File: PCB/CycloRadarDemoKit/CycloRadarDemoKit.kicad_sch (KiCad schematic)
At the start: 7 parts, among them J101 I2C conn, J102 CAN, J103 100BASE-T1, J104 Radar debug, U101 RADAR POGO pins

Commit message: starting the mockup
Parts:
- added R103: 120, Resistor_SMD:R_0603_1608Metric, symbol Device:R
- J102: footprint (none) -> Connector_Molex:Molex_39501-1003; symbol Connector_Generic:Conn_01x02 -> Connector_Generic:Conn_01x03; Mouser (none) -> 538-39501-1003
- J103: footprint (none) -> Connector_Molex:Molex_KK-254_AE-6410-04A_1x04_P2.54mm_Vertical; symbol Connector_Generic:Conn_01x02 -> Connector_Generic:Conn_01x04; Mouser (none) -> 538-34793-0040; Note (none) -> Wrong footprint
- J104: now not fitted
- U101: footprint alps_modules:ALPS Generic Radar 5 -> alps_modules:ALPS_USRR5
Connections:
- net CANH: now also J102.3 (Pin_3), R103.1; no longer J102.2 (Pin_2)
- net CANL: now also R103.2
- net ETH_H: now also J103.3 (Pin_3); no longer J103.2 (Pin_2)
- net ETH_L: now also J103.2 (Pin_2); no longer J103.1 (Pin_1)
- net GND: now also J102.2 (Pin_2)
- no-connect marks 9 -> 11
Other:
- moved on the sheet: J101, U101

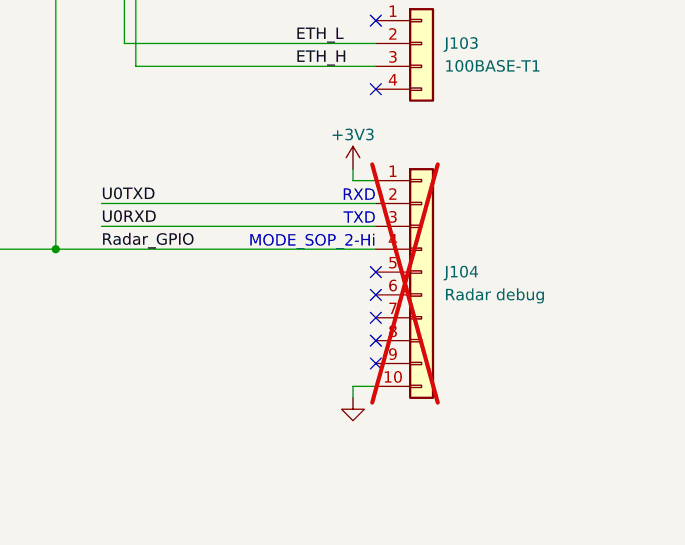
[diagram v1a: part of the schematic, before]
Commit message: layout mockup done
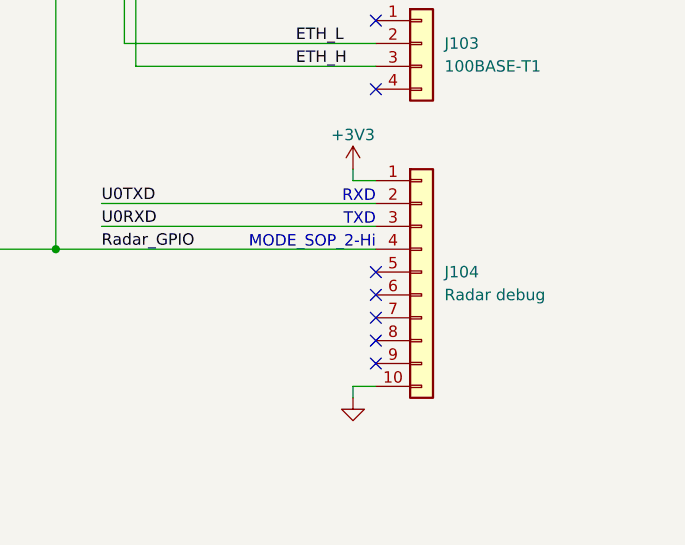
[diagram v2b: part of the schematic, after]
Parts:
- J104: now fitted
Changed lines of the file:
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@@
   )
   (symbol (lib_id "Connector_Generic:Conn_01x10") (at 257.81 135.89 0) (unit 1)
-    (in_bom yes) (on_board yes) (dnp yes) (fields_autoplaced)
+    (in_bom yes) (on_board yes) (dnp no) (fields_autoplaced)
     (property "Reference" "J104" (at 260.35 135.89 0)
       (effects (font (size 1.27 1.27)) (justify left))

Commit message: PCB, 3Dmodel
mockup PCB version done, schcematic exported to latex, 3D model generated and exported to latex
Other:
- note added: "All GND symbols refer to same ground"
- title: Safety Ride Radar Sensor -> Radar Safety Sensor
- moved on the sheet: J101, J102, J103, J104, R101, R102, R103, U101

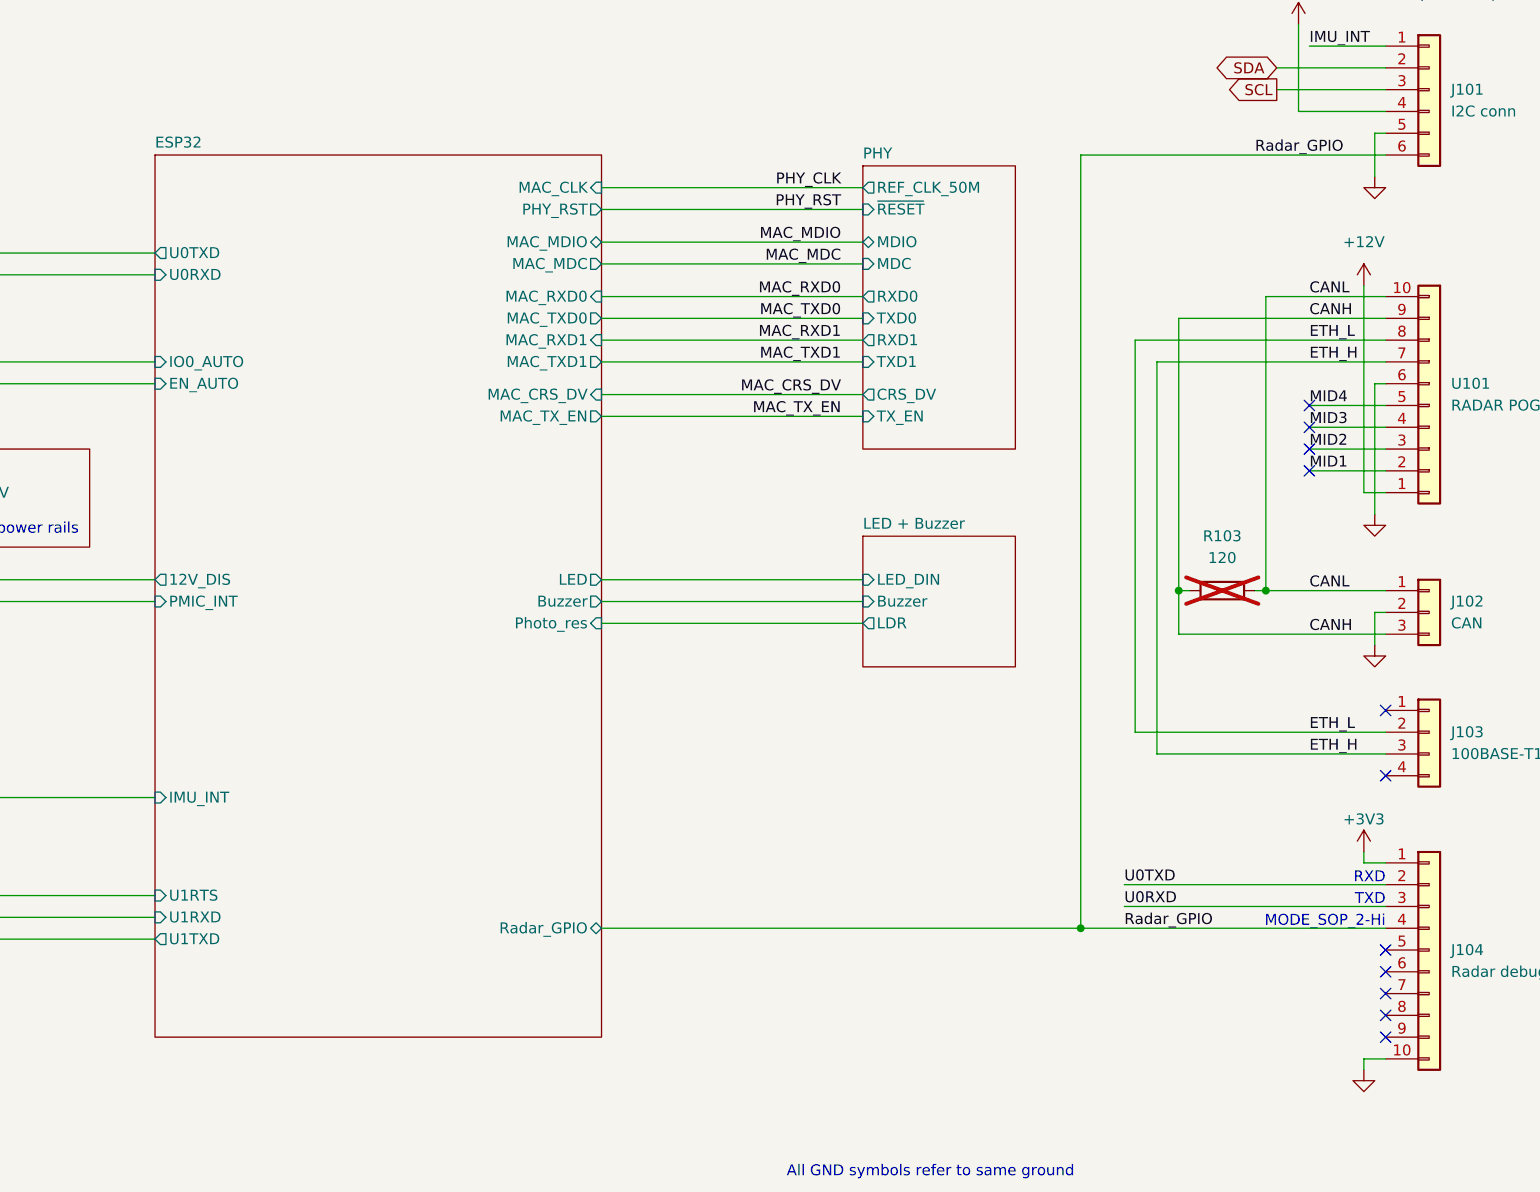
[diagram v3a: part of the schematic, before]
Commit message: sortingAbbr, cosmetics schematic, export schematic to thesis
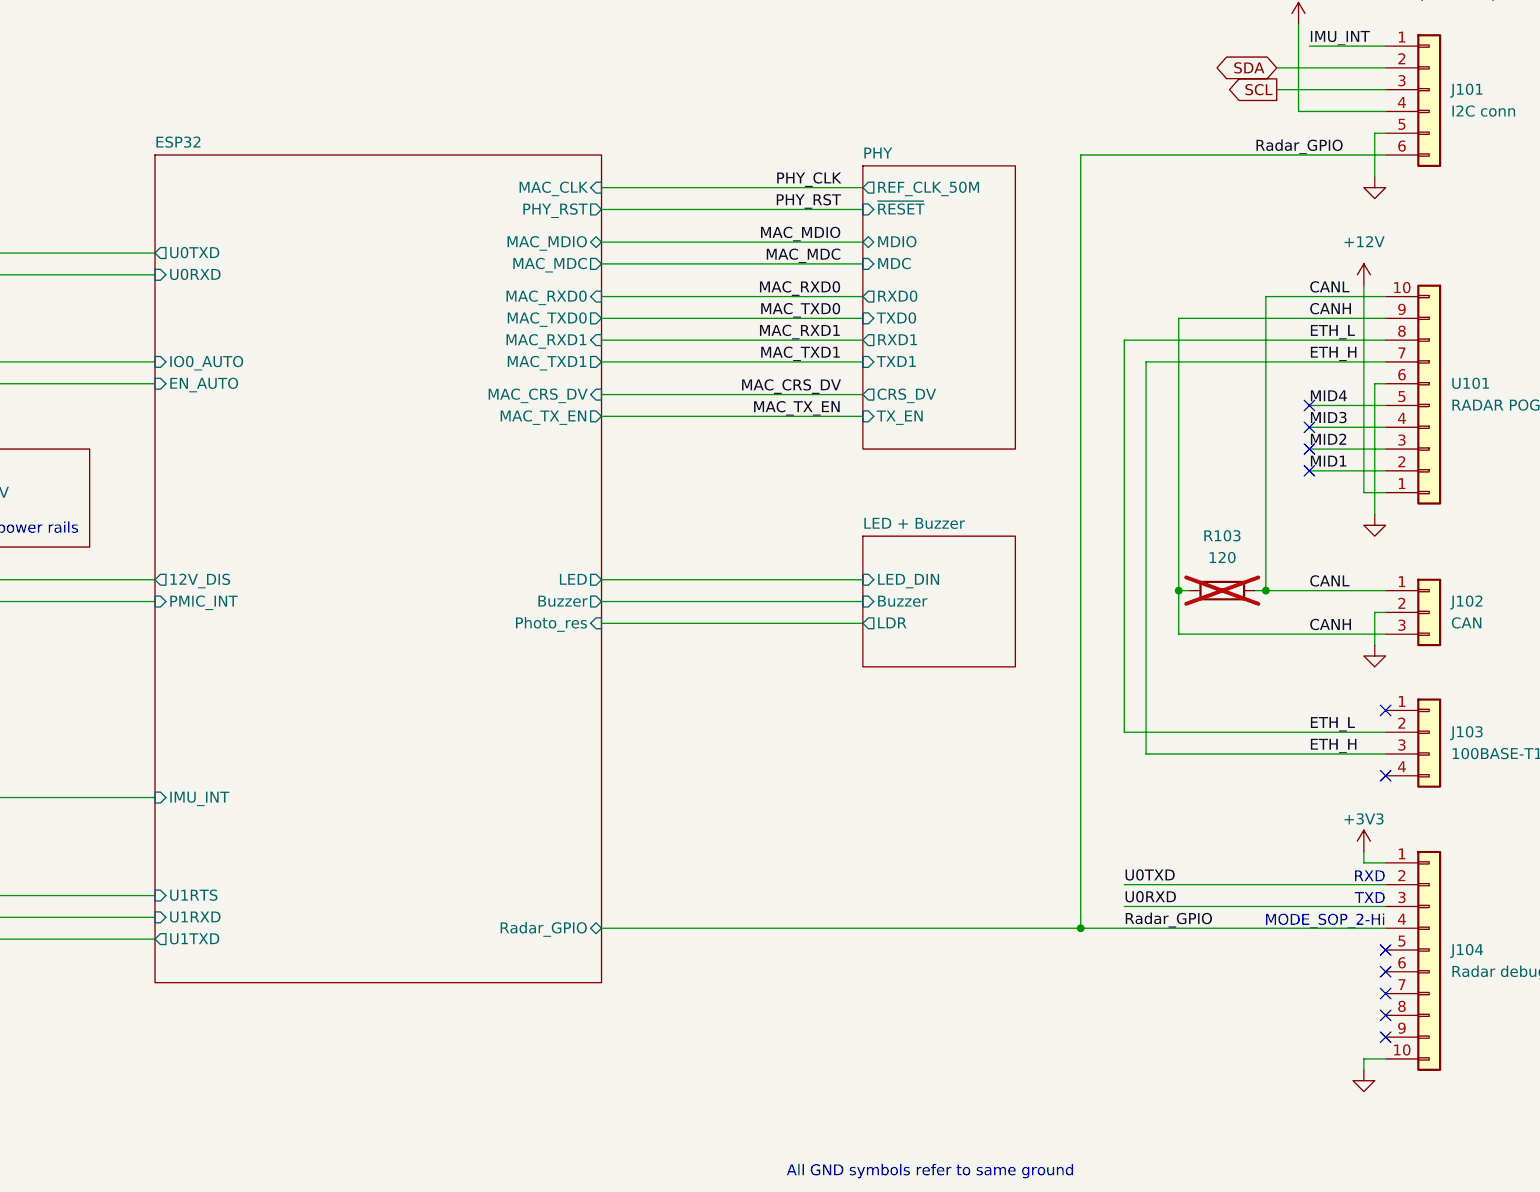
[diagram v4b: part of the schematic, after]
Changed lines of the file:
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@@
     (title "Radar Safety Sensor")
     (date "2023-12-20")
-    (rev "Rev.: 1")
+    (rev "Rev.: 1.0")
     (company "ALPS Electric Czech, s.r.o.")
     (comment 1 "Designed by Martin Tavoda")
@@
     (stroke (width 0) (type default))
   )
-  (wire (pts (xy 217.17 111.76) (xy 246.38 111.76))
+  (wire (pts (xy 215.9 111.76) (xy 246.38 111.76))
     (stroke (width 0) (type default))
   )
@@
     (stroke (width 0) (type default))
   )
-  (wire (pts (xy 219.71 114.3) (xy 219.71 68.58))
+  (wire (pts (xy 218.44 114.3) (xy 218.44 68.58))
     (stroke (width 0) (type default))
   )
@@
     (stroke (width 0) (type default))
   )
-  (wire (pts (xy 217.17 111.76) (xy 217.17 66.04))
+  (wire (pts (xy 215.9 111.76) (xy 215.9 66.04))
     (stroke (width 0) (type default))
   )
@@
     (stroke (width 0) (type default))
   )
-  (wire (pts (xy 219.71 68.58) (xy 246.38 68.58))
+  (wire (pts (xy 218.44 68.58) (xy 246.38 68.58))
     (stroke (width 0) (type default))
   )
@@
     (stroke (width 0) (type default))
   )
-  (wire (pts (xy 217.17 66.04) (xy 246.38 66.04))
+  (wire (pts (xy 215.9 66.04) (xy 246.38 66.04))
     (stroke (width 0) (type default))
   )
@@
     (stroke (width 0) (type default))
   )
-  (wire (pts (xy 219.71 114.3) (xy 246.38 114.3))
+  (wire (pts (xy 218.44 114.3) (xy 246.38 114.3))
     (stroke (width 0) (type default))
   )
@@
     )
   )
-  (sheet (at 102.87 44.45) (size 52.07 102.87) (fields_autoplaced)
+  (sheet (at 102.87 44.45) (size 52.07 96.52) (fields_autoplaced)
     (stroke (width 0.1524) (type solid))
     (fill (color 0 0 0 0.1000))
@@
       (effects (font (size 1.27 1.27)) (justify left bottom))
     )
-    (property "Sheetfile" "ESP32.kicad_sch" (at 102.87 147.9046 0)
+    (property "Sheetfile" "ESP32.kicad_sch" (at 102.87 141.5546 0)
       (effects (font (size 1.27 1.27)) (justify left top) hide)
     )
@@
     (instances
       (project "CycloRadarDemoKit"
-        (path "/c2cd7ca4-4652-4b3d-a3a8-1cfa66cb11e9" (page "8"))
+        (path "/c2cd7ca4-4652-4b3d-a3a8-1cfa66cb11e9" (page "2"))
       )
     )
@@
     (instances
       (project "CycloRadarDemoKit"
-        (path "/c2cd7ca4-4652-4b3d-a3a8-1cfa66cb11e9" (page "7"))
+        (path "/c2cd7ca4-4652-4b3d-a3a8-1cfa66cb11e9" (page "8"))
       )
     )
@@
     (instances
       (project "CycloRadarDemoKit"
-        (path "/c2cd7ca4-4652-4b3d-a3a8-1cfa66cb11e9" (page "2"))
+        (path "/c2cd7ca4-4652-4b3d-a3a8-1cfa66cb11e9" (page "3"))
       )
     )
@@
     (instances
       (project "CycloRadarDemoKit"
-        (path "/c2cd7ca4-4652-4b3d-a3a8-1cfa66cb11e9" (page "4"))
+        (path "/c2cd7ca4-4652-4b3d-a3a8-1cfa66cb11e9" (page "7"))
       )
     )
@@
     (instances
       (project "CycloRadarDemoKit"
-        (path "/c2cd7ca4-4652-4b3d-a3a8-1cfa66cb11e9" (page "5"))
+        (path "/c2cd7ca4-4652-4b3d-a3a8-1cfa66cb11e9" (page "4"))
       )
     )
@@
     (instances
       (project "CycloRadarDemoKit"
-        (path "/c2cd7ca4-4652-4b3d-a3a8-1cfa66cb11e9" (page "3"))
+        (path "/c2cd7ca4-4652-4b3d-a3a8-1cfa66cb11e9" (page "6"))
       )
     )
@@
     (instances
       (project "CycloRadarDemoKit"
-        (path "/c2cd7ca4-4652-4b3d-a3a8-1cfa66cb11e9" (page "6"))
-      )
-    )
+        (path "/c2cd7ca4-4652-4b3d-a3a8-1cfa66cb11e9" (page "5"))
+      )
+    )

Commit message: PCB small updates, schemtatic cosmetics, SEP FINAL
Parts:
- added H101, H102, H103, H104: MountingHole, MountingHole:MountingHole_2.7mm_M2.5_ISO7380, symbol Mechanical:MountingHole
- J103: footprint Connector_Molex:Molex_KK-254_AE-6410-04A_1x04_P2.54mm_Vertical -> Connector_Molex:Molex_347920040; Mouser 538-34793-0040 -> 538-34792-0040; Note Wrong footprint -> (none)
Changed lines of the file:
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@@
+    )
+  )
+  (symbol (lib_id "Mechanical:MountingHole") (at 167.64 178.435 90) (mirror x) (unit 1)
+    (in_bom no) (on_board yes) (dnp no) (fields_autoplaced)
+    (property "Reference" "H102" (at 165.1 177.165 90)
+      (effects (font (size 1.27 1.27)) (justify left))
+    )
+    (property "Value" "MountingHole" (at 165.1 179.705 90)
+      (effects (font (size 1.27 1.27)) (justify left))
+    )
+    (property "Footprint" "MountingHole:MountingHole_2.7mm_M2.5_ISO7380" (at 167.64 178.435 0)
+      (effects (font (size 1.27 1.27)) hide)
+    )
+    (property "Datasheet" "~" (at 167.64 178.435 0)
+      (effects (font (size 1.27 1.27)) hide)
+    )
+    (instances
+      (project "CycloRadarDemoKit"
+        (path "/c2cd7ca4-4652-4b3d-a3a8-1cfa66cb11e9"
+          (reference "H102") (unit 1)
+        )
+      )
     )
   )
@@
         (path "/c2cd7ca4-4652-4b3d-a3a8-1cfa66cb11e9"
           (reference "J102") (unit 1)
+        )
+      )
+    )
+  )
+  (symbol (lib_id "Mechanical:MountingHole") (at 167.64 172.72 90) (mirror x) (unit 1)
+    (in_bom no) (on_board yes) (dnp no) (fields_autoplaced)
+    (property "Reference" "H101" (at 165.1 171.45 90)
+      (effects (font (size 1.27 1.27)) (justify left))
+    )
+    (property "Value" "MountingHole" (at 165.1 173.99 90)
+      (effects (font (size 1.27 1.27)) (justify left))
+    )
+    (property "Footprint" "MountingHole:MountingHole_2.7mm_M2.5_ISO7380" (at 167.64 172.72 0)
+      (effects (font (size 1.27 1.27)) hide)
+    )
+    (property "Datasheet" "~" (at 167.64 172.72 0)
+      (effects (font (size 1.27 1.27)) hide)
+    )
+    (instances
+      (project "CycloRadarDemoKit"
+        (path "/c2cd7ca4-4652-4b3d-a3a8-1cfa66cb11e9"
+          (reference "H101") (unit 1)
         )
       )
@@
     )
   )
+  (symbol (lib_id "Mechanical:MountingHole") (at 167.64 184.15 90) (mirror x) (unit 1)
+    (in_bom no) (on_board yes) (dnp no) (fields_autoplaced)
+    (property "Reference" "H103" (at 165.1 182.88 90)
+      (effects (font (size 1.27 1.27)) (justify left))
+    )
+    (property "Value" "MountingHole" (at 165.1 185.42 90)
+      (effects (font (size 1.27 1.27)) (justify left))
+    )
+    (property "Footprint" "MountingHole:MountingHole_2.7mm_M2.5_ISO7380" (at 167.64 184.15 0)
+      (effects (font (size 1.27 1.27)) hide)
+    )
+    (property "Datasheet" "~" (at 167.64 184.15 0)
+      (effects (font (size 1.27 1.27)) hide)
+    )
+    (instances
+      (project "CycloRadarDemoKit"
+        (path "/c2cd7ca4-4652-4b3d-a3a8-1cfa66cb11e9"
+          (reference "H103") (unit 1)
+        )
+      )
+    )
+  )
   (symbol (lib_id "power:+3V3") (at 243.84 125.73 0) (unit 1)
     (in_bom yes) (on_board yes) (dnp no)
@@
         (path "/c2cd7ca4-4652-4b3d-a3a8-1cfa66cb11e9"
           (reference "#PWR0105") (unit 1)
+        )
+      )
+    )
+  )
+  (symbol (lib_id "Mechanical:MountingHole") (at 167.64 189.865 90) (mirror x) (unit 1)
+    (in_bom no) (on_board yes) (dnp no) (fields_autoplaced)
+    (property "Reference" "H104" (at 165.1 188.595 90)
+      (effects (font (size 1.27 1.27)) (justify left))
+    )
+    (property "Value" "MountingHole" (at 165.1 191.135 90)
+      (effects (font (size 1.27 1.27)) (justify left))
+    )
+    (property "Footprint" "MountingHole:MountingHole_2.7mm_M2.5_ISO7380" (at 167.64 189.865 0)
+      (effects (font (size 1.27 1.27)) hide)
+    )
+    (property "Datasheet" "~" (at 167.64 189.865 0)
+      (effects (font (size 1.27 1.27)) hide)
+    )
+    (instances
+      (project "CycloRadarDemoKit"
+        (path "/c2cd7ca4-4652-4b3d-a3a8-1cfa66cb11e9"
+          (reference "H104") (unit 1)
         )
       )
@@
       (effects (font (size 1.27 1.27)) (justify left))
     )
-    (property "Footprint" "Connector_Molex:Molex_KK-254_AE-6410-04A_1x04_P2.54mm_Vertical" (at 251.46 111.76 0)
+    (property "Footprint" "Connector_Molex:Molex_347920040" (at 251.46 111.76 0)
       (effects (font (size 1.27 1.27)) hide)
     )
@@
       (effects (font (size 1.27 1.27)) hide)
     )
-    (property "Mouser" "538-34793-0040" (at 251.46 111.76 0)
-      (effects (font (size 1.27 1.27)) hide)
-    )
-    (property "Note" "Wrong footprint" (at 251.46 111.76 0)
-      (effects (font (size 1.27 1.27)) hide)
-    )
+    (property "Mouser" "538-34792-0040" (at 251.46 111.76 0)
+      (effects (font (size 1.27 1.27)) hide)
+    )

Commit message: UART tested
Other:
- note added: "!!! TODO: Chech the GPIO purpose: GPIO for I2C GPIO for INT UART1 OK GPIO for ADC OK GPIO 4 LED OK GPIO 33 OK"
- note removed: "!!! TODO: Chech the GPIO purpose: UART1 GPIO for I2C GPIO for INT GPIO for ADC OK GPIO 4 LED OK GPIO 33 OK"
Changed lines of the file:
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@@
     (effects (font (size 1.27 1.27) (color 0 0 0 1)) (justify right bottom))
   )
-  (text "!!! TODO: Chech the GPIO purpose:\nUART1 \nGPIO for I2C\nGPIO for INT\n\nGPIO for ADC OK\nGPIO 4 LED OK\nGPIO 33 OK"
+  (text "!!! TODO: Chech the GPIO purpose:\nGPIO for I2C\nGPIO for INT\n\nUART1 OK\nGPIO for ADC OK\nGPIO 4 LED OK\nGPIO 33 OK"
     (at 346.71 19.05 0)
     (effects (font (size 1.27 1.27)) (justify right bottom))

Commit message: All peripherals checked, changed ESP32 pinout
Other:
- note removed: "!!! TODO: Chech the GPIO purpose: GPIO for I2C GPIO for INT UART1 OK GPIO for ADC OK GPIO 4 LED OK GPIO 33 OK"
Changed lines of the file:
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@@
     (effects (font (size 1.27 1.27) (color 0 0 0 1)) (justify right bottom))
-  )
-  (text "!!! TODO: Chech the GPIO purpose:\nGPIO for I2C\nGPIO for INT\n\nUART1 OK\nGPIO for ADC OK\nGPIO 4 LED OK\nGPIO 33 OK"
-    (at 346.71 19.05 0)
-    (effects (font (size 1.27 1.27)) (justify right bottom))
   )
   (text "Global power rails" (at 53.34 102.87 0)
@@
       (effects (font (size 1.27 1.27)) (justify right))
     )
-    (pin "U1RTS" input (at 102.87 130.81 180)
+    (pin "U1RTS" output (at 102.87 130.81 180)
       (effects (font (size 1.27 1.27)) (justify left))
     )
@@
       (effects (font (size 1.27 1.27)) (justify right))
     )
-    (pin "PMIC_PV" input (at 54.61 96.52 0)
+    (pin "PMIC_PV" output (at 54.61 96.52 0)
       (effects (font (size 1.27 1.27)) (justify right))
     )
@@
       (effects (font (size 1.27 1.27)) (justify right))
     )
-    (pin "RTS" output (at 54.61 130.81 0)
-      (effects (font (size 1.27 1.27)) (justify right))
-    )
+    (pin "RTS" input (at 54.61 130.81 0)
+      (effects (font (size 1.27 1.27)) (justify right))
+    )
